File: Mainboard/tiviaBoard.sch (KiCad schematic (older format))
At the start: 1 part, among them J1 Ti_Booster_40

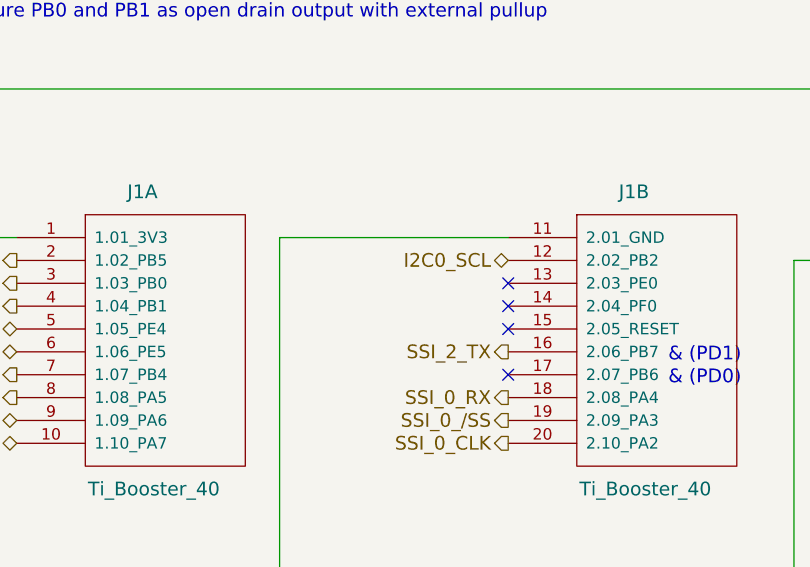
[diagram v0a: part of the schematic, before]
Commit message: Updated Schematic with minor changes after first prototype
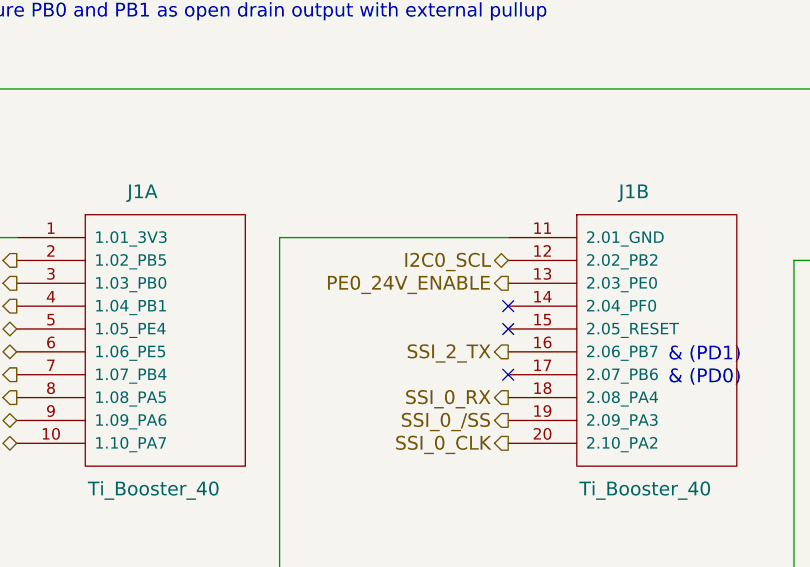
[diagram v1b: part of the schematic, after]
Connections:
- net labels added: PE0_24V_ENABLE
- no-connect marks 7 -> 6
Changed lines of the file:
@@
 32 A5 BE 09 BA 48 21 C5 E2 65 A5 D9 BC 20 6B 5B B8 83 64 B2 21 D0 C4 D6 7D F8 03 B3 59 26 1D 1E
 7F 93 77 53 7B B5 9A 53 C8 EA 92 4D 52 88 29 49 6C C6 A2 96 0D 0D 05 A4 F0 FF 83 88 FF 0B 96 8F
-AE AD C3 83 87 45 00 00 00 00 49 45 4E 44 AE 42 60 82 00
+AE AD C3 83 87 45 00 00 00 00 49 45 4E 44 AE 42 60 82 A4
 EndData
 $EndBitmap
@@
 61 20 10 88 FF 08 E8 4A 06 02 81 40 20 10 08 95 80 5E F5 8E 40 20 10 08 04 42 25 A0 45 06 02 81
 40 20 10 08 95 80 16 19 08 04 02 81 40 20 54 C2 FF 01 D3 55 27 F0 0D 6A 9E 83 00 00 00 00 49 45
-4E 44 AE 42 60 82 4E
+4E 44 AE 42 60 82 00
 EndData
 $EndBitmap
@@
 po_{0-3}_pwm = M0PWM{0-3}
 NoConn ~ 6200 2100
-NoConn ~ 3800 1900
 NoConn ~ 3800 2000
 Text Notes 900  750  0    60   ~ 0
@@
 	1    0    0    -1
 $EndComp
+Text HLabel 3800 1900 0    60   Output ~ 0
+PE0_24V_ENABLE
 $EndSCHEMATC
